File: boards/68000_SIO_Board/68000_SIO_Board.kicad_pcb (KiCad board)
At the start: 2 copper layers, 101.6 x 55.9 mm, 32 parts, among them J1 Conn_01x08, J10 Conn_02x08_Odd_Even, J11 Conn_01x08, J12 Conn_02x04_Odd_Even, J13 Conn_01x10, J14 Conn_02x02_Odd_Even, J2 Conn_01x06, J3 Conn_01x03, J4 Conn_02x10_Odd_Even, J5 Conn_01x06, J6 Conn_01x03, J7 Conn_01x06, J8 Conn_01x06, J9 Conn_01x08, M1 RC2014_40_PIN, U1 74LS138, U2 68681P, U3 68681P, X1 CXO_DIP8

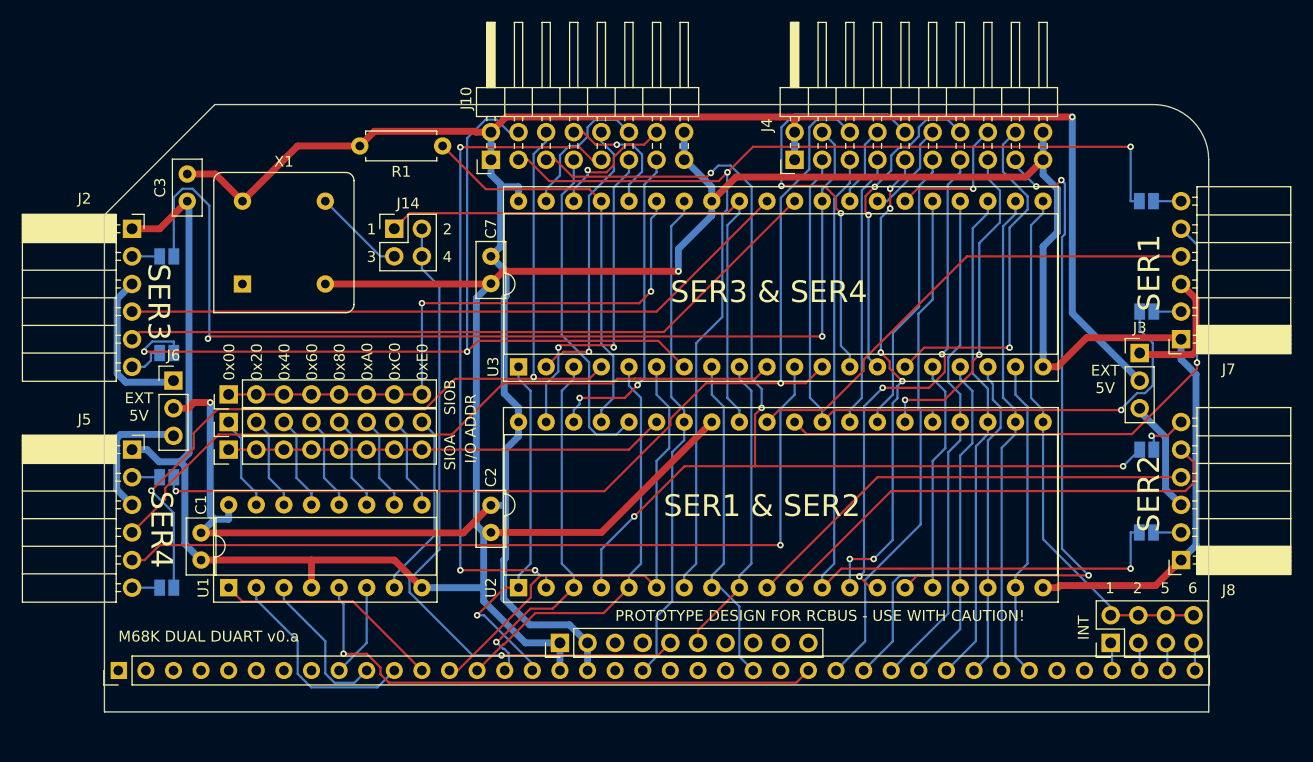
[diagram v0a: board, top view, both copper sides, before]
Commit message: Update to v2 board set
Lots of updates to reflect the new v2 boards that use the full RCBus 80 pins as well as slight modifications to the various test programs to reflect the new IO and MEM space addresses.
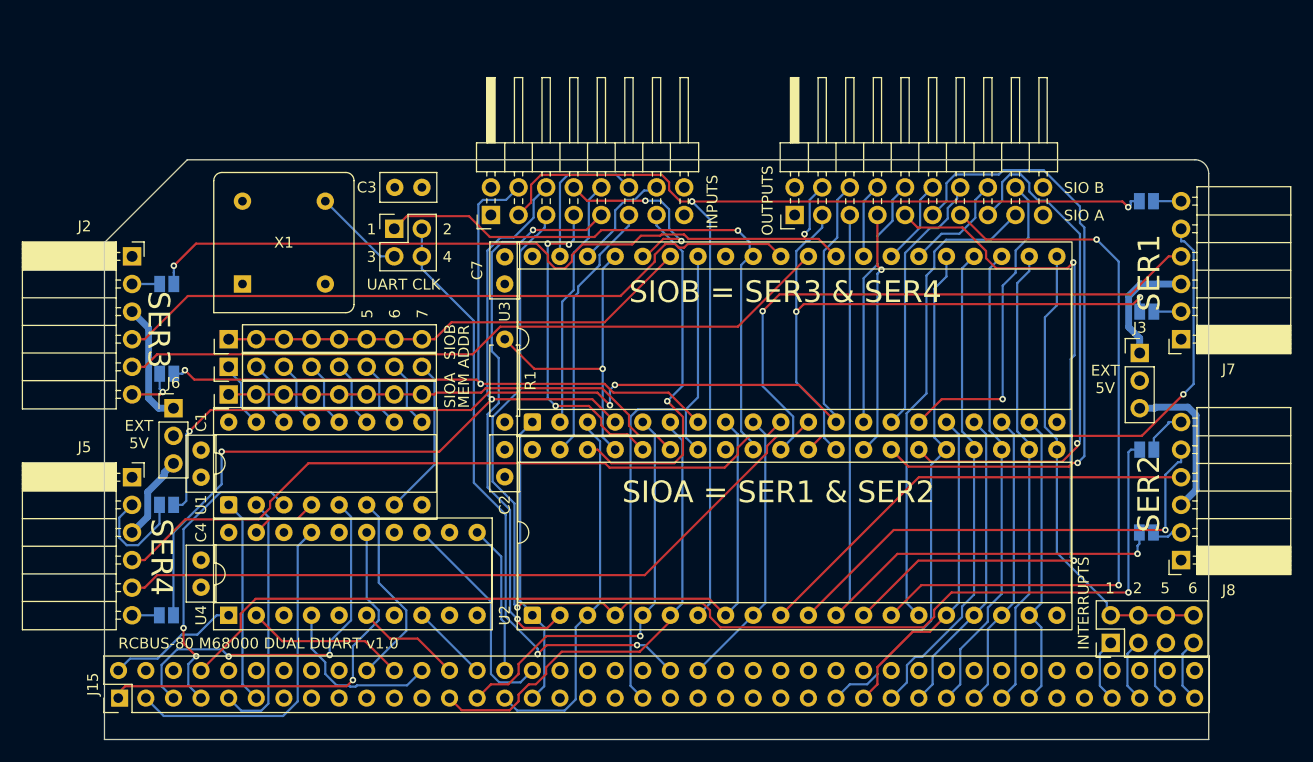
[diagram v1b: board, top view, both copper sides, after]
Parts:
- removed J13: Conn_01x10, Connector_PinHeader_2.54mm:PinHeader_1x10_P2.54mm_Vertical
- removed M1: RC2014_40_PIN, MyLibrary2023:RC2014_STD_40_PIN
- added C4: 100n, Capacitor_THT:C_Disc_D5.0mm_W2.5mm_P2.50mm, F.Cu at (92.7, 106.6)
- added J15: RCBus_80PIN_68000, MyLibrary2023:RCBus_80p_Medium, F.Cu at (83.8, 120.7)
- added U4: 74LS688, MyLibrary2023:DIP-20_W7.62mm_Socket, F.Cu at (95.2, 109.2)
- moved C3 21.6 mm to (113.0, 69.8), turned to 180 degrees
- moved R1 18.7 mm to (120.7, 83.8), turned to -90 degrees
- moved C1 7.62 mm to (92.7, 96.5)
- moved U1 7.62 mm to (95.2, 99.1)
- moved C2 5.28 mm to (120.7, 96.5)
- moved U3 5.24 mm to (123.2, 91.4)
- moved J11 5.08 mm to (95.2, 83.8)
- moved J1 5.08 mm to (95.2, 86.4)
- moved J10 5.08 mm to (119.4, 72.4)
- moved J4 5.08 mm to (147.3, 72.4)
- moved J9 5.08 mm to (95.2, 88.9)
- moved U2 2.84 mm to (123.2, 109.2)
- moved JP7 2.54 mm to (89.5, 109.2)
- moved JP8 2.54 mm to (89.5, 99.1)
- moved J2 2.54 mm to (86.4, 76.2)
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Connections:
- net /~{WR} renamed /R/~{W}
- net Net-(U2-IACK) renamed /~{IACK}
- U1 pad 1: /A5 -> /A11
- U1 pad 2: /A6 -> /A12
- U1 pad 3: /A7 -> /A13
- U1 pad 4: GND -> Net-(U1-E1)
- U1 pad 5: /~{IORQ} -> /A14
- U1 pad 6: /A8 -> /A23
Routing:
- net GND: track 293.2 -> 0.00 mm, vias 1 -> 0
- net +5V: track 224.8 -> 0.00 mm, vias 2 -> 0
- net /~{IORQ}: track 51.0 -> 0.00 mm, vias 1 -> 0
- net /R/~{W}: track 31.2 -> 71.3 mm
- net /A16: track 0.00 -> 37.6 mm, vias 0 -> 1
- net /A14: track 0.00 -> 35.0 mm, vias 0 -> 2
- net /OPA4: track 26.2 -> 59.6 mm, vias 0 -> 1
- net /A15: track 0.00 -> 31.3 mm
- net /A13: track 0.00 -> 27.9 mm, vias 0 -> 2
- net /OPB0: track 98.3 -> 72.6 mm
- net /A12: track 0.00 -> 23.2 mm
- net /OPA3: track 44.4 -> 67.3 mm, vias 6 -> 2
- net /OPA5: track 47.0 -> 68.2 mm, vias 3 -> 2
- net /A5: track 20.9 -> 0.00 mm
- net /A17: track 0.00 -> 20.2 mm
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- added copper zone on In1.Cu, net +5V
- added copper zone on In2.Cu, net GND
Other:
- board size 101.6 x 55.9 mm -> 101.6 x 53.3 mm
- copper layers 2 -> 4
- board text added: "7"
- board text added: "CS0"
- board text added: "CS0: $D00000 CS4: $D02000 CS1: $D00800 CS5: $D02800 CS2: $D01000 CS6: $D03000 CS3: $D01800 CS7: $D03800"
- board text added: "CS1"
- board text added: "CS2"
- board text added: "CS3"
- board text added: "CS4"
- board text added: "CS5"
- board text added: "CS6"
- board text added: "CS7"
- board text added: "INPUTS"
- board text added: "INTERRUPTS"
- board text added: "JLCJLCJLCJLC"
- board text added: "MEM ADDR"
- board text added: "OUTPUTS"
- board text added: "RCBUS-80 M68000 DUAL DUART v1.0"
- board text added: "SET EXT5V JUMPER TO POWER SYSTEM FROM SERIAL PORT"
- board text added: "SIO A"
- board text added: "SIO B"
- board text added: "SIOA = SER1 & SER2"
- board text added: "SIOB = SER3 & SER4"
- board text added: "UART CLK"
- board text added: "UART CLOCK SOURCE 1-3: ON BOARD OSC 1-2: EXT CLOCK 1-2 & 3-4 : ON BOARD OSC + SUPPLY EXT CLOCK"
- board text removed: "0x00"
- board text removed: "0x20"
- board text removed: "0x40"
- board text removed: "0x60"
- board text removed: "0x80"
- board text removed: "0xA0"
- board text removed: "0xC0"
- board text removed: "0xE0"
- board text removed: "I/O ADDR"
- board text removed: "INT"
- board text removed: "M68K DUAL DUART v0.a"
- board text removed: "PROTOTYPE DESIGN FOR RCBUS - USE WITH CAUTION!"
- board text removed: "SER1 & SER2"
- board text removed: "SER3 & SER4"
